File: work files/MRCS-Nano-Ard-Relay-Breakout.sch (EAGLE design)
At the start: 20 parts, among them CON1 5V PWR, J1 5V PWR, J2 Unused I/O

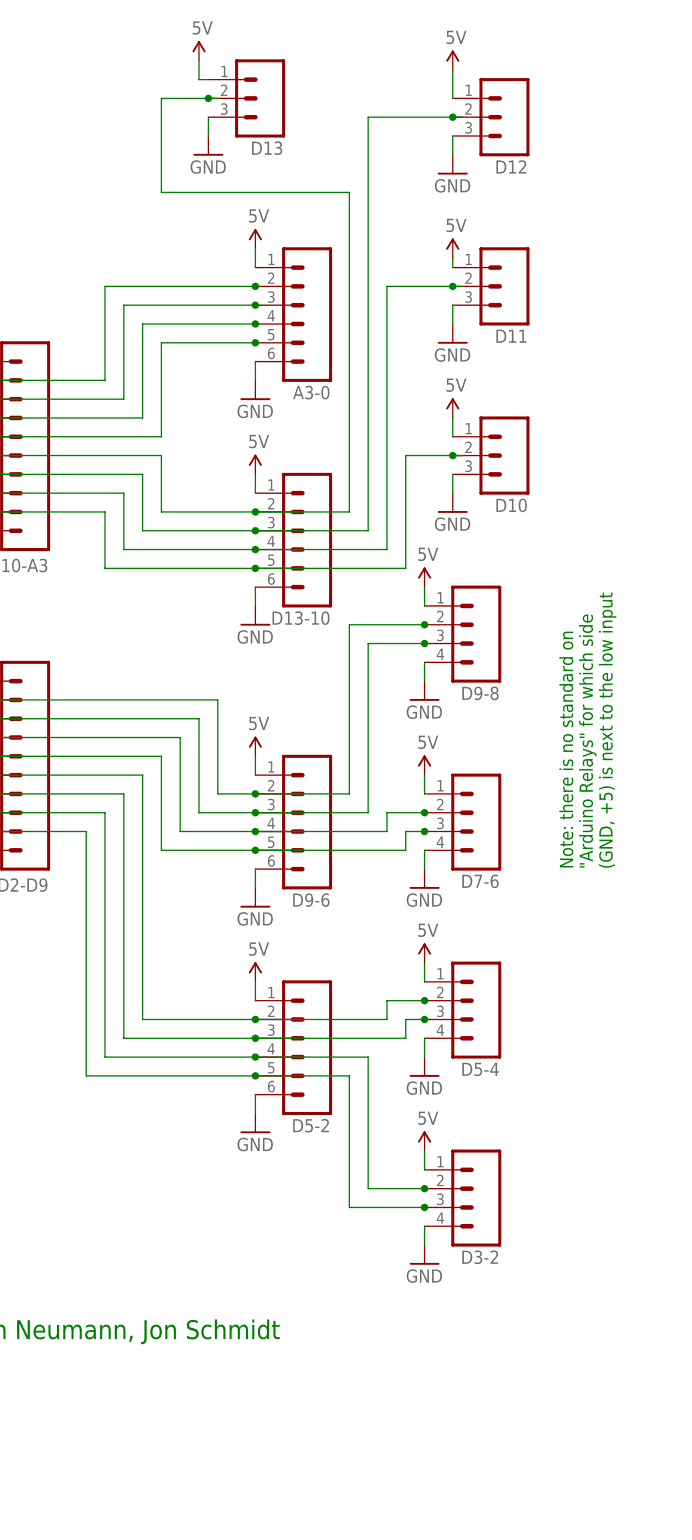
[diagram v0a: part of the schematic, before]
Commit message: fixed connectors 8 and 16 position Arduino Relays
accidently selected 2mm rather than 2.54mm (0.100) connectors.  Fixed positions of the singlets (different pattern of course).
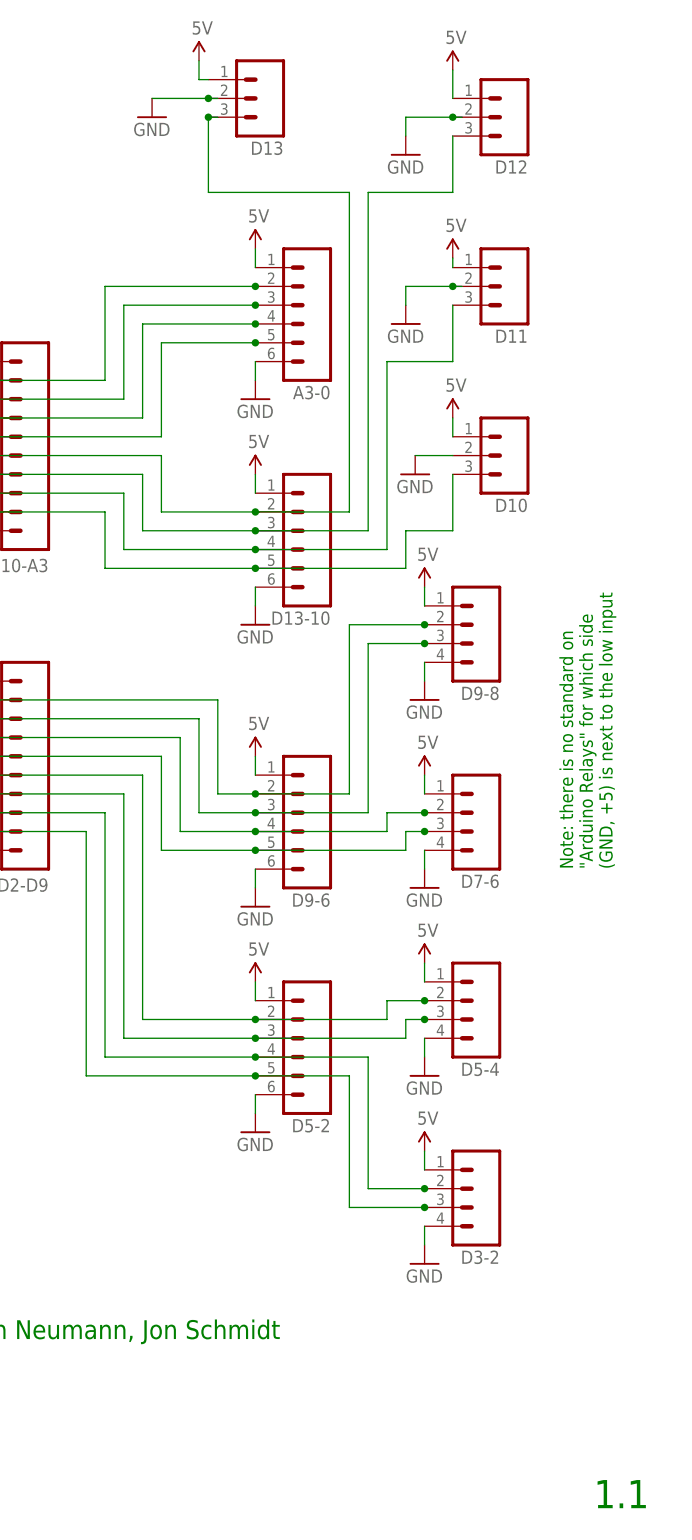
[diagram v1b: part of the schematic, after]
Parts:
- D10-A3, D2-D9: value CONNECTOR-M102MM -> CONNECTOR-M10LOCK; device SPCoast:CONNECTOR-M102MM -> SPCoast:CONNECTOR-M10LOCK
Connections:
- net GND: now also D10.2, D11.2, D12.2, D13.2; no longer D10.3, D11.3, D12.3, D13.3
- net N$11: now also D10.3; no longer D10.2
- net N$12: now also D11.3; no longer D11.2
- net N$13: now also D12.3; no longer D12.2
- net N$14: now also D13.3; no longer D13.2
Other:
- note added: "1.1"
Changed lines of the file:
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@@
 <part name="J2" library="SPCoast" deviceset="CONNECTOR-M08" device="LOCK" value="Unused I/O"/>
 <part name="GND8" library="SparkFun-Aesthetics" deviceset="GND" device=""/>
-<part name="D2-D9" library="SPCoast" deviceset="CONNECTOR-M10" device="2MM"/>
-<part name="D10-A3" library="SPCoast" deviceset="CONNECTOR-M10" device="2MM"/>
+<part name="D2-D9" library="SPCoast" deviceset="CONNECTOR-M10" device="LOCK" value="CONNECTOR-M10LOCK"/>
+<part name="D10-A3" library="SPCoast" deviceset="CONNECTOR-M10" device="LOCK" value="CONNECTOR-M10LOCK"/>
 <part name="A3-0" library="SPCoast" deviceset="CONNECTOR-M06" device="LOCK"/>
 <part name="D13-10" library="SPCoast" deviceset="CONNECTOR-M06" device="LOCK"/>
@@
 "Arduino Relays" for which side
 (GND, +5) is next to the low input</text>
+<text x="238.76" y="-5.08" size="3.81" layer="91">1.1</text>
 </plain>
 <instances>
@@
 <instance part="GND14" gate="1" x="215.9" y="78.74"/>
 <instance part="GND15" gate="1" x="215.9" y="104.14"/>
-<instance part="GND16" gate="1" x="219.71" y="129.54"/>
-<instance part="GND17" gate="1" x="219.71" y="152.4"/>
-<instance part="GND18" gate="1" x="219.71" y="175.26"/>
-<instance part="GND19" gate="1" x="186.69" y="177.8"/>
+<instance part="GND16" gate="1" x="214.63" y="134.62"/>
+<instance part="GND17" gate="1" x="213.36" y="154.94"/>
+<instance part="GND18" gate="1" x="213.36" y="177.8"/>
+<instance part="GND19" gate="1" x="179.07" y="182.88"/>
 <instance part="SUPPLY6" gate="G$1" x="219.71" y="142.24"/>
 <instance part="SUPPLY7" gate="G$1" x="219.71" y="163.83"/>
@@
 </segment>
 <segment>
-<pinref part="GND19" gate="1" pin="GND"/>
-<pinref part="D13" gate="G$1" pin="3"/>
-<wire x1="186.69" y1="180.34" x2="186.69" y2="182.88" width="0.6096" layer="91"/>
-</segment>
-<segment>
-<pinref part="GND18" gate="1" pin="GND"/>
-<pinref part="D12" gate="G$1" pin="3"/>
-<wire x1="219.71" y1="177.8" x2="219.71" y2="180.34" width="0.6096" layer="91"/>
-</segment>
-<segment>
-<pinref part="GND17" gate="1" pin="GND"/>
-<pinref part="D11" gate="G$1" pin="3"/>
-<wire x1="219.71" y1="154.94" x2="219.71" y2="157.48" width="0.6096" layer="91"/>
-</segment>
-<segment>
-<pinref part="GND16" gate="1" pin="GND"/>
-<pinref part="D10" gate="G$1" pin="3"/>
-<wire x1="219.71" y1="132.08" x2="219.71" y2="134.62" width="0.6096" layer="91"/>
-</segment>
-<segment>
 <pinref part="D5-4" gate="J" pin="4"/>
 <pinref part="GND13" gate="1" pin="GND"/>
@@
 <pinref part="GND8" gate="1" pin="GND"/>
 <wire x1="38.1" y1="109.22" x2="60.96" y2="109.22" width="0.6096" layer="91"/>
+</segment>
+<segment>
+<pinref part="GND19" gate="1" pin="GND"/>
+<wire x1="179.07" y1="185.42" x2="186.69" y2="185.42" width="0.3048" layer="91"/>
+<pinref part="D13" gate="G$1" pin="2"/>
+<wire x1="186.69" y1="185.42" x2="187.96" y2="185.42" width="0.3048" layer="91"/>
+<junction x="186.69" y="185.42"/>
+</segment>
+<segment>
+<pinref part="GND16" gate="1" pin="GND"/>
+<pinref part="D10" gate="G$1" pin="2"/>
+<wire x1="214.63" y1="137.16" x2="219.71" y2="137.16" width="0.6096" layer="91"/>
+</segment>
+<segment>
+<wire x1="220.98" y1="160.02" x2="219.71" y2="160.02" width="0.3048" layer="91"/>
+<pinref part="GND17" gate="1" pin="GND"/>
+<wire x1="219.71" y1="160.02" x2="213.36" y2="160.02" width="0.3048" layer="91"/>
+<wire x1="213.36" y1="160.02" x2="213.36" y2="157.48" width="0.3048" layer="91"/>
+<pinref part="D11" gate="G$1" pin="2"/>
+<junction x="219.71" y="160.02"/>
+</segment>
+<segment>
+<wire x1="220.98" y1="182.88" x2="219.71" y2="182.88" width="0.3048" layer="91"/>
+<pinref part="GND18" gate="1" pin="GND"/>
+<wire x1="219.71" y1="182.88" x2="213.36" y2="182.88" width="0.3048" layer="91"/>
+<wire x1="213.36" y1="182.88" x2="213.36" y2="180.34" width="0.3048" layer="91"/>
+<pinref part="D12" gate="G$1" pin="2"/>
+<junction x="219.71" y="182.88"/>
 </segment>
 </net>
@@
 <wire x1="172.72" y1="121.92" x2="193.04" y2="121.92" width="0.3048" layer="91"/>
 <wire x1="193.04" y1="121.92" x2="213.36" y2="121.92" width="0.3048" layer="91"/>
-<wire x1="213.36" y1="121.92" x2="213.36" y2="137.16" width="0.3048" layer="91"/>
-<wire x1="213.36" y1="137.16" x2="219.71" y2="137.16" width="0.3048" layer="91"/>
-<pinref part="D10" gate="G$1" pin="2"/>
-<wire x1="219.71" y1="137.16" x2="220.98" y2="137.16" width="0.3048" layer="91"/>
-<junction x="219.71" y="137.16"/>
+<wire x1="213.36" y1="121.92" x2="213.36" y2="127" width="0.3048" layer="91"/>
 <junction x="154.94" y="129.54"/>
 <junction x="193.04" y="121.92"/>
+<wire x1="213.36" y1="127" x2="219.71" y2="127" width="0.3048" layer="91"/>
+<pinref part="D10" gate="G$1" pin="3"/>
+<wire x1="219.71" y1="127" x2="219.71" y2="134.62" width="0.3048" layer="91"/>
 </segment>
 </net>
@@
 <wire x1="175.26" y1="124.46" x2="193.04" y2="124.46" width="0.3048" layer="91"/>
 <wire x1="193.04" y1="124.46" x2="210.82" y2="124.46" width="0.3048" layer="91"/>
-<wire x1="210.82" y1="124.46" x2="210.82" y2="160.02" width="0.3048" layer="91"/>
-<wire x1="210.82" y1="160.02" x2="219.71" y2="160.02" width="0.3048" layer="91"/>
-<pinref part="D11" gate="G$1" pin="2"/>
-<wire x1="219.71" y1="160.02" x2="220.98" y2="160.02" width="0.3048" layer="91"/>
-<junction x="219.71" y="160.02"/>
+<wire x1="210.82" y1="124.46" x2="210.82" y2="149.86" width="0.3048" layer="91"/>
 <junction x="154.94" y="132.08"/>
 <junction x="193.04" y="124.46"/>
+<wire x1="210.82" y1="149.86" x2="219.71" y2="149.86" width="0.3048" layer="91"/>
+<pinref part="D11" gate="G$1" pin="3"/>
+<wire x1="219.71" y1="149.86" x2="219.71" y2="157.48" width="0.3048" layer="91"/>
 </segment>
 </net>
@@
 <wire x1="177.8" y1="127" x2="193.04" y2="127" width="0.3048" layer="91"/>
 <wire x1="193.04" y1="127" x2="208.28" y2="127" width="0.3048" layer="91"/>
-<wire x1="208.28" y1="127" x2="208.28" y2="182.88" width="0.3048" layer="91"/>
-<wire x1="208.28" y1="182.88" x2="219.71" y2="182.88" width="0.3048" layer="91"/>
-<pinref part="D12" gate="G$1" pin="2"/>
-<wire x1="219.71" y1="182.88" x2="220.98" y2="182.88" width="0.3048" layer="91"/>
-<junction x="219.71" y="182.88"/>
+<wire x1="208.28" y1="127" x2="208.28" y2="172.72" width="0.3048" layer="91"/>
 <pinref part="D10-A3" gate="G$1" pin="7"/>
 <junction x="154.94" y="134.62"/>
 <junction x="193.04" y="127"/>
+<wire x1="208.28" y1="172.72" x2="219.71" y2="172.72" width="0.3048" layer="91"/>
+<pinref part="D12" gate="G$1" pin="3"/>
+<wire x1="219.71" y1="172.72" x2="219.71" y2="180.34" width="0.3048" layer="91"/>
 </segment>
 </net>
@@
 <wire x1="193.04" y1="129.54" x2="205.74" y2="129.54" width="0.3048" layer="91"/>
 <wire x1="205.74" y1="129.54" x2="205.74" y2="172.72" width="0.3048" layer="91"/>
-<wire x1="205.74" y1="172.72" x2="180.34" y2="172.72" width="0.3048" layer="91"/>
-<wire x1="180.34" y1="172.72" x2="180.34" y2="185.42" width="0.3048" layer="91"/>
-<wire x1="180.34" y1="185.42" x2="186.69" y2="185.42" width="0.3048" layer="91"/>
+<wire x1="205.74" y1="172.72" x2="186.69" y2="172.72" width="0.3048" layer="91"/>
 <junction x="154.94" y="137.16"/>
-<pinref part="D13" gate="G$1" pin="2"/>
-<wire x1="186.69" y1="185.42" x2="187.96" y2="185.42" width="0.3048" layer="91"/>
-<junction x="186.69" y="185.42"/>
 <junction x="193.04" y="129.54"/>
-</segment>
-</net>
+<wire x1="187.96" y1="182.88" x2="186.69" y2="182.88" width="0.3048" layer="91"/>
+<wire x1="186.69" y1="182.88" x2="186.69" y2="172.72" width="0.3048" layer="91"/>
+<pinref part="D13" gate="G$1" pin="3"/>
+<junction x="186.69" y="182.88"/>
+</segment>
+</net>
